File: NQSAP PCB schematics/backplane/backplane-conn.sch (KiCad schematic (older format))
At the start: 8 parts, among them J11 Bus, J12 Bus, J13 Bus, J14 Bus, J15 Bus, J16 Bus, J17 Bus, J18 Bus

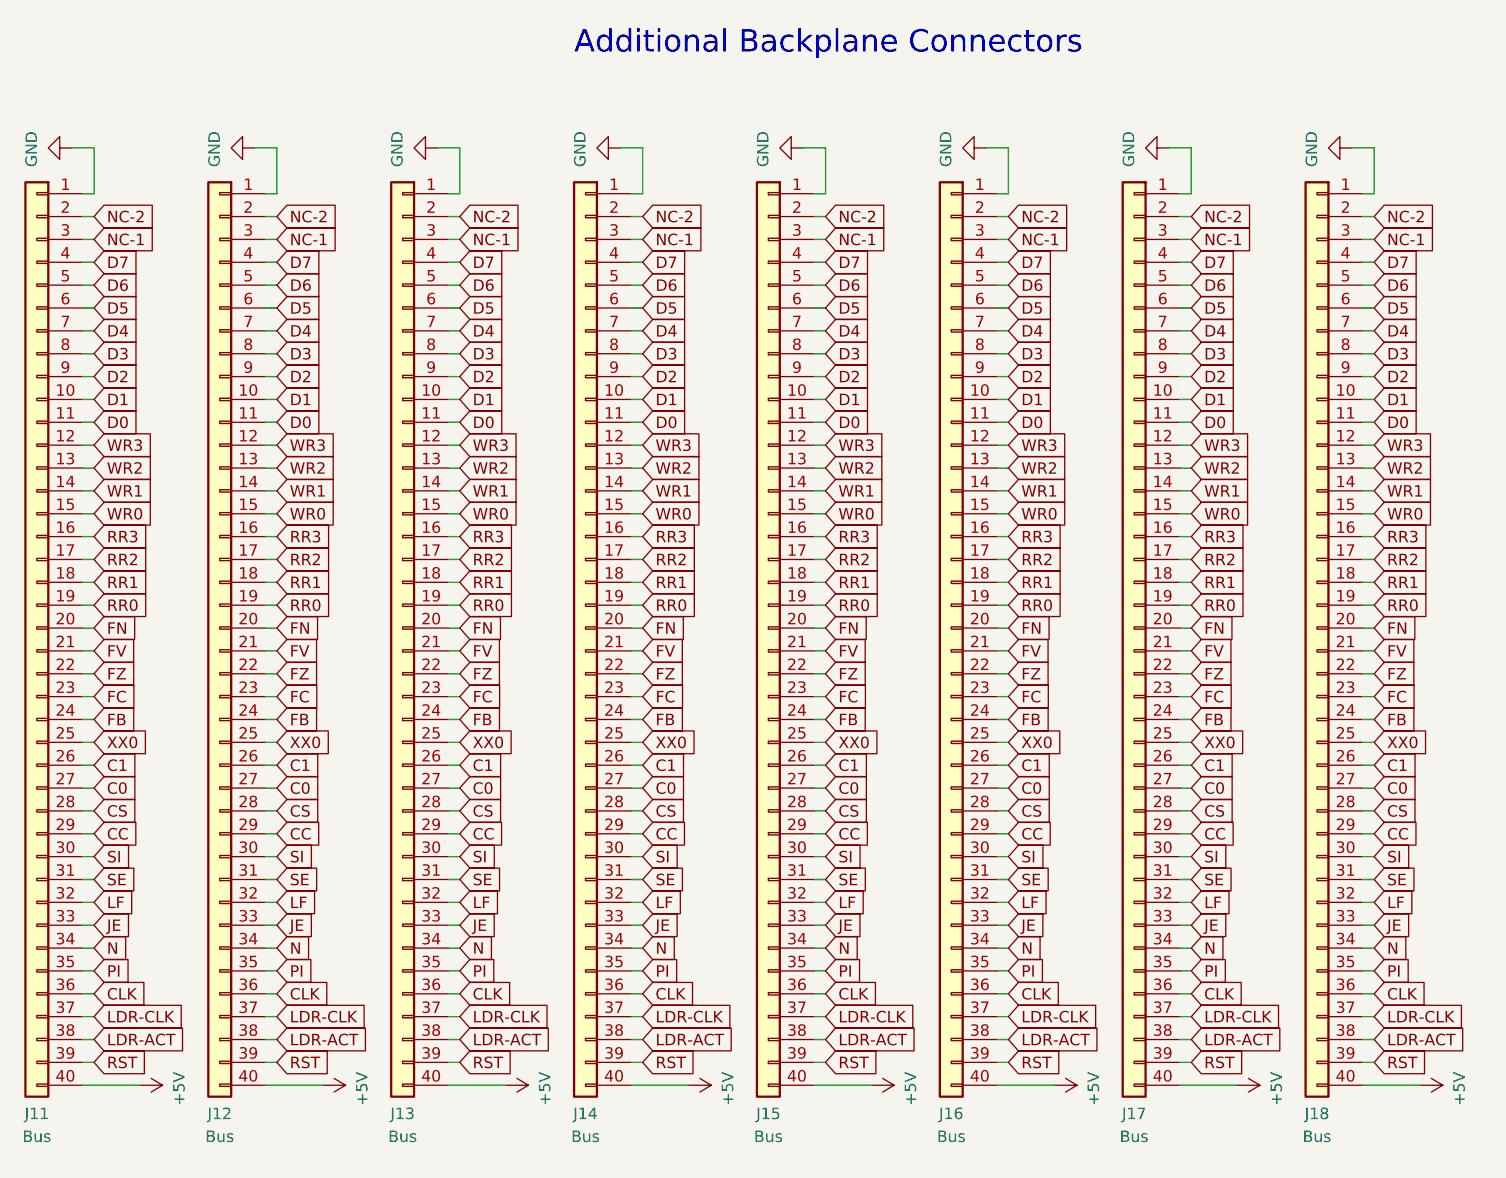
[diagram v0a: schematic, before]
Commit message: Add RAM, update and add gerbers for new boards
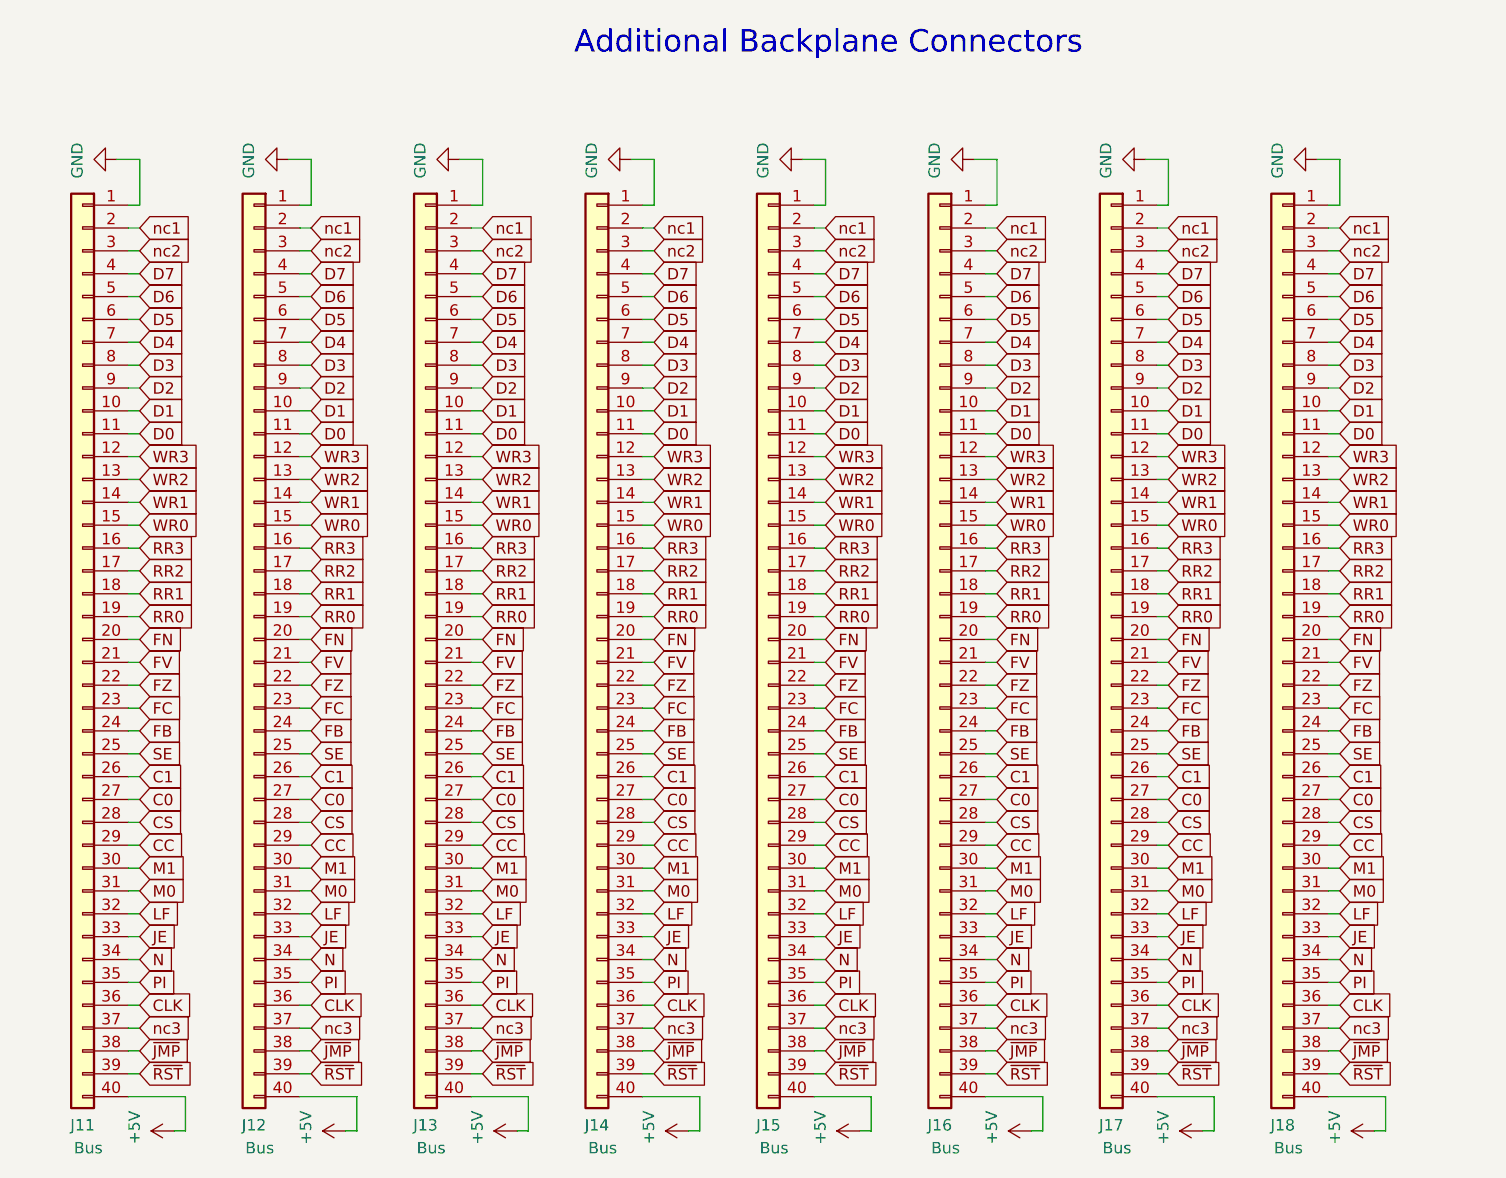
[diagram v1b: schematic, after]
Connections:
- net XX0 is gone; now on net SE: J11.25 (Pin_25), J12.25 (Pin_25), J13.25 (Pin_25), J14.25 (Pin_25), J15.25 (Pin_25), J16.25 (Pin_25), J17.25 (Pin_25), J18.25 (Pin_25)
- net SE: no longer J11.31 (Pin_31), J12.31 (Pin_31), J13.31 (Pin_31), J14.31 (Pin_31), J15.31 (Pin_31), J16.31 (Pin_31), J17.31 (Pin_31), J18.31 (Pin_31)
- net LDR-ACT renamed ~JMP
- net LDR-CLK renamed nc3
- net NC-1 renamed nc2
- net NC-2 renamed nc1
- net RST renamed ~RST
- net SI renamed M1
- new net M0: J11.31 (Pin_31), J12.31 (Pin_31), J13.31 (Pin_31), J14.31 (Pin_31), J15.31 (Pin_31), J16.31 (Pin_31), J17.31 (Pin_31), J18.31 (Pin_31)
